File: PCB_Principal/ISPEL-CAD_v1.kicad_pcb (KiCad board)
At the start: 2 copper layers, 130 x 160 mm, 173 parts, among them J1 Vin, J10 E1, J11 S1, J12 E2, J13 S2, J14 FRENTE, J15 PRUEBA_5V, J16 V5, J17 VREG, J2 GND_NUCLEO, J3 CN8_NUCLEO, J4 CN9_NUCLEO, J5 GND_NUCLEO, J6 GND_NUCLEO, J7 CN7_NUCLEO, J8 CN10_NUCLEO, J9 GND_NUCLEO, Q201 BC807, Q202 BC559C, Q203 BC549C, Q204 BC549C, Q205 BC559C, Q206 2SD882, Q207 2SB772, Q251 BC807, Q252 BC559C, Q253 BC549C, Q254 BC549C, Q255 BC559C, Q256 2SD882, Q257 2SB772, U1 LM350_TO220, U101 TL071, U151 TL071, U2 LM350_TO220, U201 LM318, U251 LM318, U3 LM337_TO220, U301 TLV3501AID, U4 LM1117DT-5.0, U5 TL431DBZ

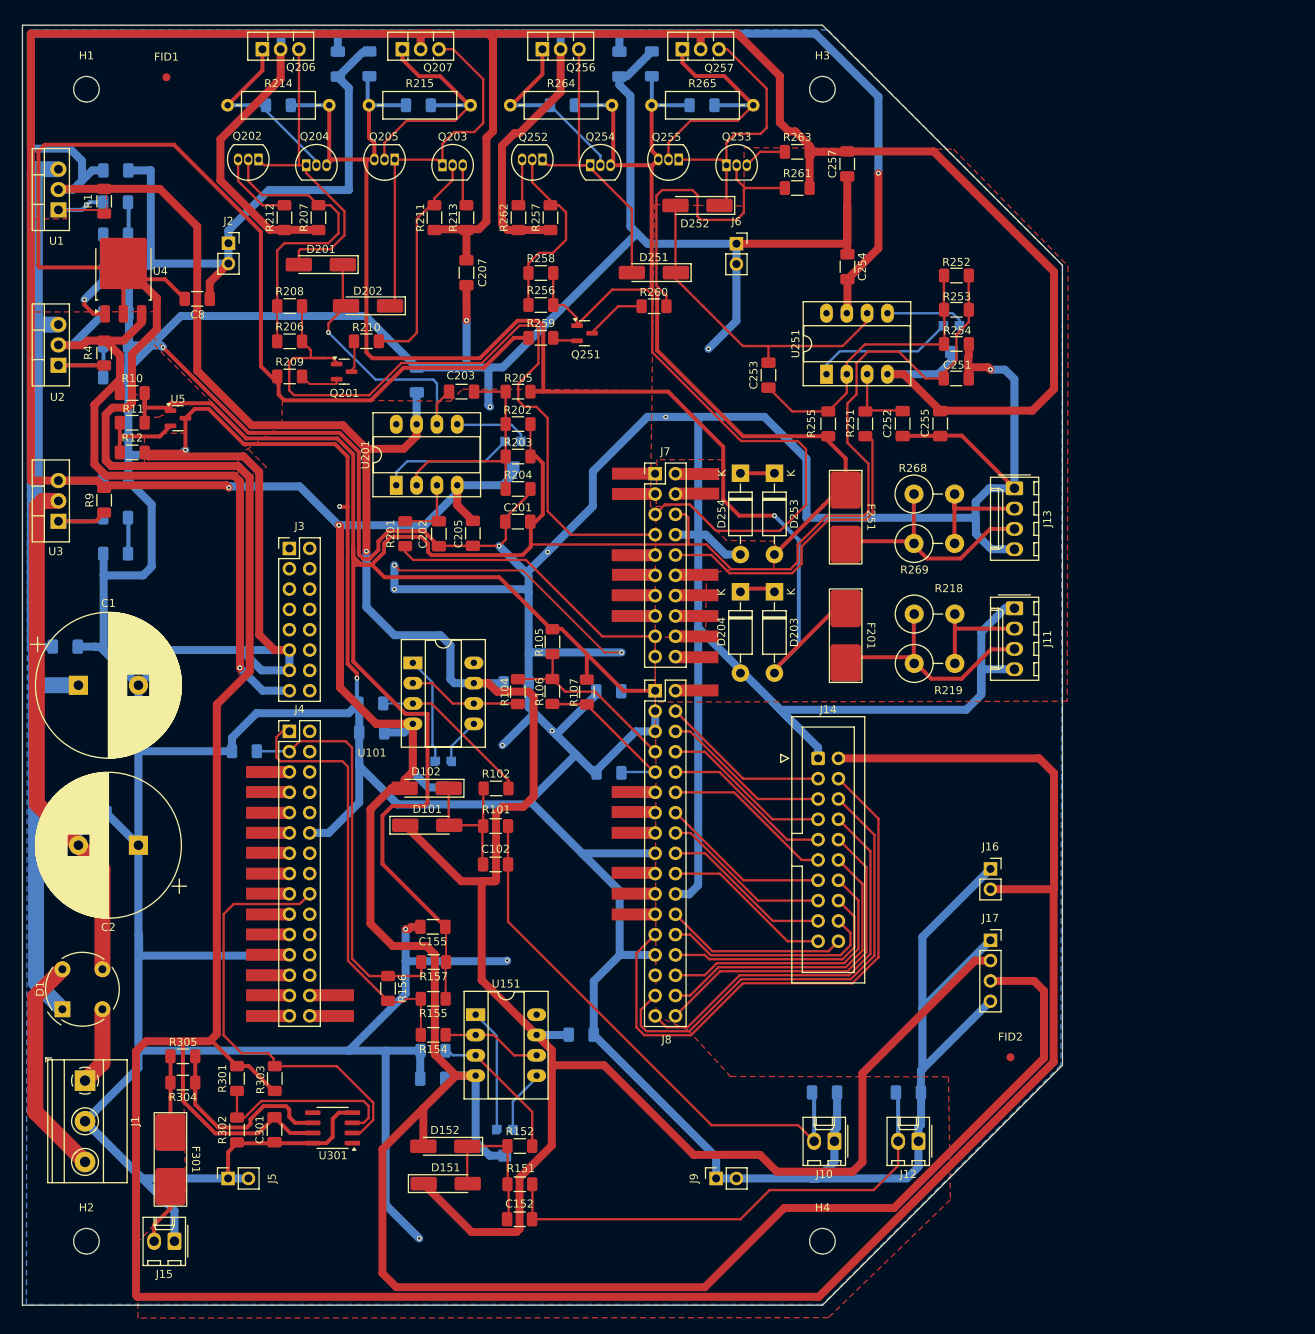
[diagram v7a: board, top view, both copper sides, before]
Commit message: Agregado de leyendas y pin para sensor de temperatura.
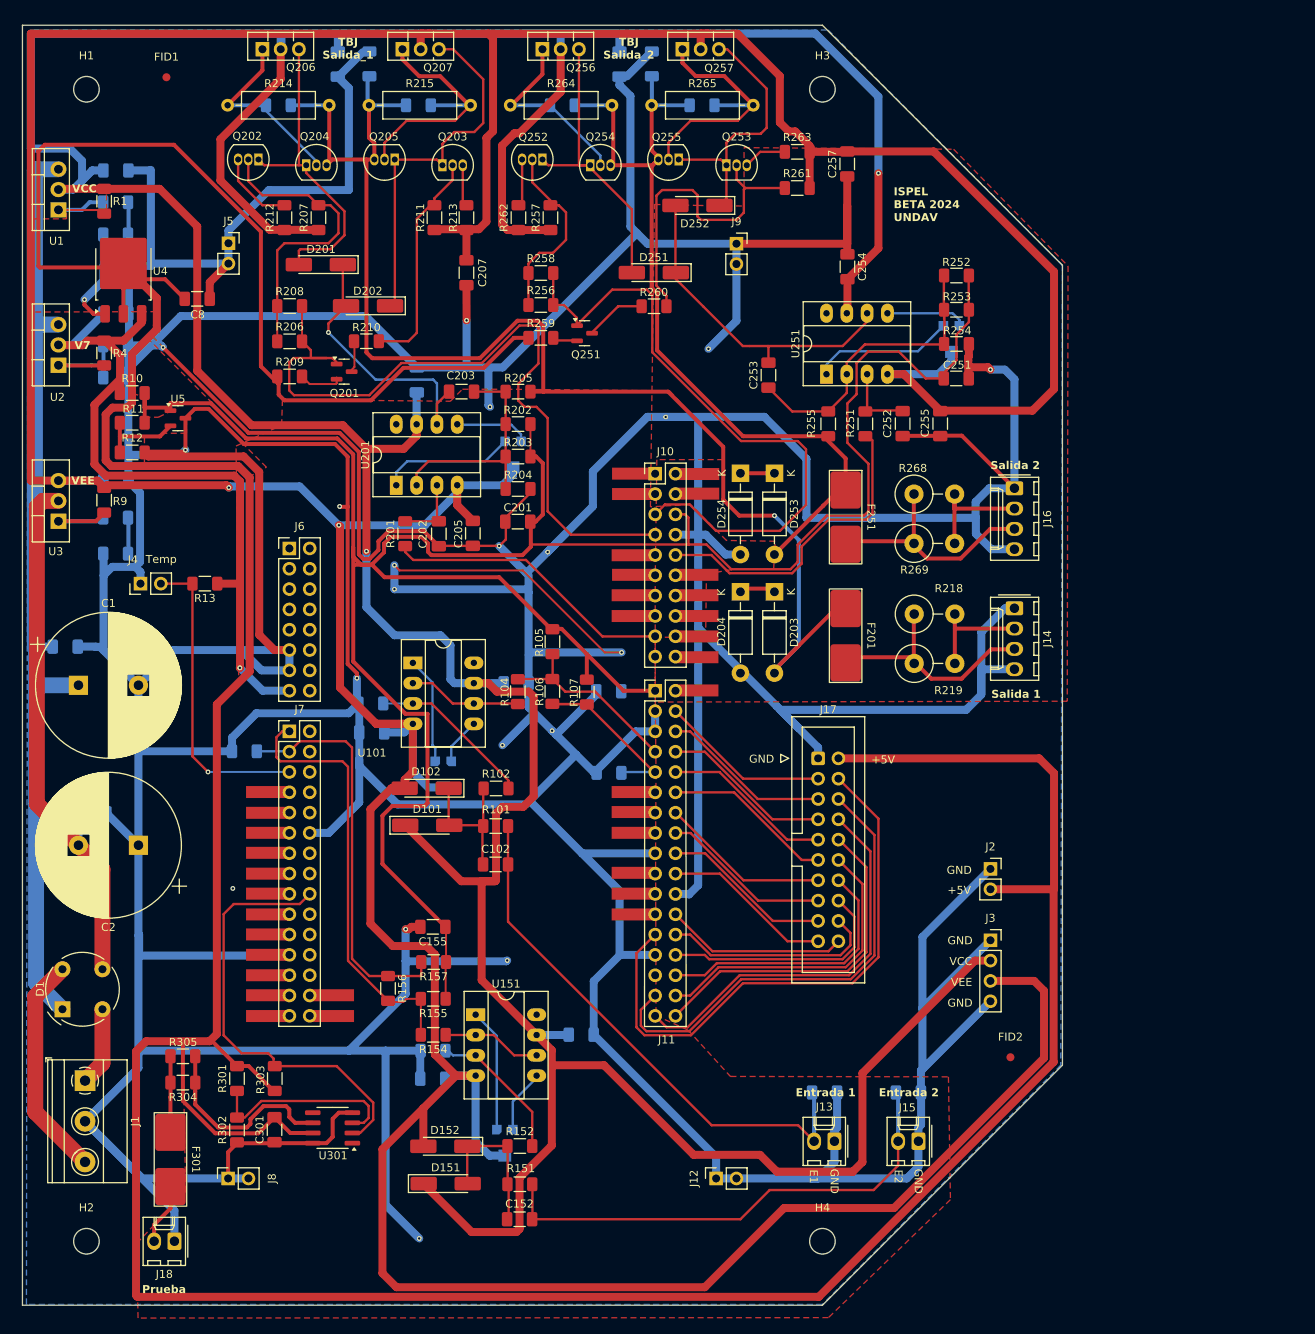
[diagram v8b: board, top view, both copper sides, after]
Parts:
- added J4: TEMP, Connector_PinHeader_2.54mm:PinHeader_1x02_P2.54mm_Vertical, F.Cu at (44.8, 99.8)
- added R13: 4K7, Resistor_SMD:R_1206_3216Metric_Pad1.30x1.75mm_HandSolder, F.Cu at (52.8, 99.8)
- renumbered J7 to J10, J8 to J11, J9 to J12, J10 to J13, J11 to J14, J12 to J15, J13 to J16, J14 to J17, J15 to J18, J16 to J2, J17 to J3, J2 to J5, J3 to J6, J4 to J7, J5 to J8, J6 to J9
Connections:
- J7 pad 5: unconnected-(J4-Pin_5-Pad5) -> ADC_NTC
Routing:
- net ADC_NTC: track 0.00 -> 38.5 mm, vias 0 -> 1
- net V7: track 89.1 -> 91.9 mm
- net GND: vias 20 -> 21
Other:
- board text added: "+5V"
- board text added: "E1"
- board text added: "E2"
- board text added: "Entrada 1"
- board text added: "Entrada 2"
- board text added: "GND"
- board text added: "ISPEL BETA 2024 UNDAV"
- board text added: "Prueba"
- board text added: "Salida 1"
- board text added: "Salida 2"
- board text added: "TBJ Salida_1"
- board text added: "TBJ Salida_2"
- board text added: "Temp"
- board text added: "V7"
- board text added: "VCC"
- board text added: "VEE"
